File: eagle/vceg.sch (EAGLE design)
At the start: 58 parts, among them IC1 4052N, IC2 4001N, IC3 TL074P, IC4 CA3080E, Q1 2N3906INLINE, Q2 2N3906INLINE, U1 POWER

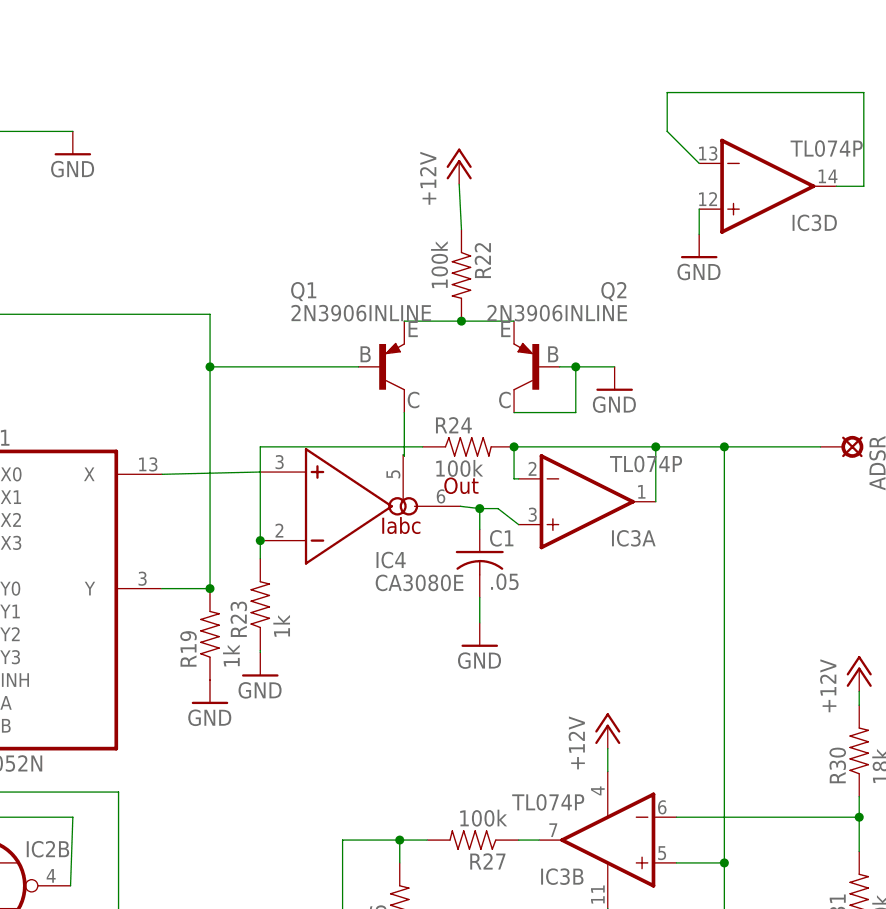
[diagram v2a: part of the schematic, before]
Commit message: ca3080 with power now
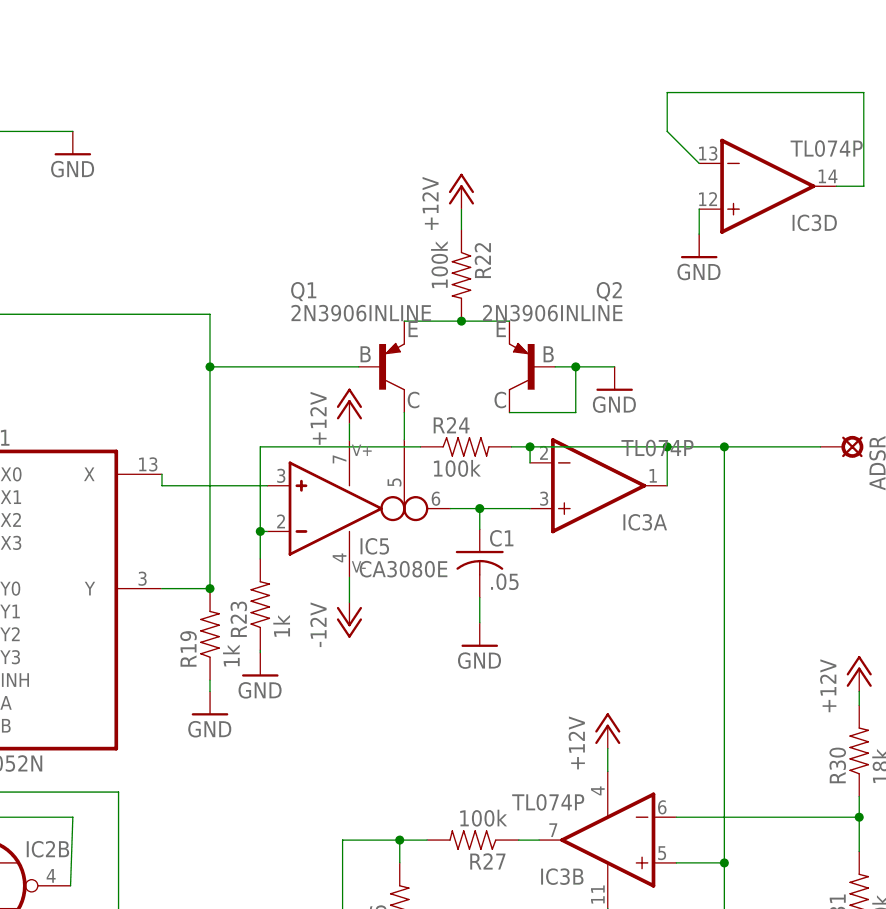
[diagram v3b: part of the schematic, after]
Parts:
- removed IC4: CA3080E, synthdiy:CA3080E
- added IC5: CA3080E, ota:CA3080E
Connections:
- removed net N$23: IC4.IABC, Q1.C
- new net N$41: IC1A.X, IC5G$1.IN_P
- net +12V: now also IC5G$2.V+
- net -12V: now also IC5G$2.V-
- net N$21: now also IC5G$1.I_BIAS, Q1.C; no longer IC1A.X, IC4.+IN
- net N$24: now also IC5G$1.IN_N; no longer IC4.-IN
- net N$28: now also IC5G$1.OUT; no longer IC4.OUT
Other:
- moved on the sheet: IC3A, Q2
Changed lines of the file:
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@@
 <part name="GND11" library="supply1" deviceset="GND" device=""/>
 <part name="R21" library="SparkFun-Resistors" deviceset="RESISTOR" device="PTH-1/4W" value="10k"/>
-<part name="IC4" library="synthdiy" deviceset="CA3080" device="E"/>
 <part name="Q1" library="bt_transistor" deviceset="2N3906" device="INLINE"/>
 <part name="Q2" library="bt_transistor" deviceset="2N3906" device="INLINE"/>
@@
 <part name="P+12" library="supply1" deviceset="+12V" device=""/>
 <part name="P-2" library="supply1" deviceset="-12V" device=""/>
+<part name="IC5" library="ota" deviceset="CA3080" device="E"/>
+<part name="P+13" library="supply1" deviceset="+12V" device=""/>
+<part name="P-3" library="supply1" deviceset="-12V" device=""/>
 </parts>
 <sheets>
@@
 <instance part="IC2" gate="C" x="67.818" y="-14.224"/>
 <instance part="IC2" gate="D" x="91.694" y="-22.352" rot="R180"/>
-<instance part="IC3" gate="A" x="133.35" y="55.372" rot="MR180"/>
+<instance part="IC3" gate="A" x="134.62" y="57.15" rot="MR180"/>
 <instance part="IC3" gate="B" x="135.636" y="17.78" rot="R180"/>
 <instance part="IC3" gate="C" x="135.636" y="-10.922" rot="R180"/>
@@
 <instance part="GND9" gate="1" x="48.26" y="27.94"/>
 <instance part="R19" gate="G$1" x="91.44" y="40.64" rot="R90"/>
-<instance part="GND10" gate="1" x="91.44" y="33.02"/>
+<instance part="GND10" gate="1" x="91.44" y="31.75"/>
 <instance part="GATE" gate="1" x="22.86" y="-8.636" rot="R90"/>
 <instance part="R20" gate="G$1" x="25.4" y="-16.51" rot="R90"/>
 <instance part="GND11" gate="1" x="25.4" y="-27.178"/>
 <instance part="R21" gate="G$1" x="37.592" y="12.7" rot="R180"/>
-<instance part="IC4" gate="G$1" x="107.188" y="54.864" rot="MR180"/>
 <instance part="Q1" gate="G$1" x="110.49" y="70.358"/>
-<instance part="Q2" gate="G$1" x="127.762" y="70.358" rot="MR0"/>
+<instance part="Q2" gate="G$1" x="127.254" y="70.358" rot="MR0"/>
 <instance part="R22" gate="G$1" x="119.38" y="80.518" rot="R270"/>
-<instance part="P+8" gate="1" x="119.126" y="93.218"/>
+<instance part="P+8" gate="1" x="119.38" y="90.424"/>
 <instance part="R23" gate="G$1" x="97.028" y="43.942" rot="R90"/>
 <instance part="GND12" gate="1" x="97.028" y="36.068"/>
-<instance part="R24" gate="G$1" x="120.142" y="61.468"/>
+<instance part="R24" gate="G$1" x="119.888" y="61.468"/>
 <instance part="C1" gate="G$1" x="121.412" y="49.784"/>
 <instance part="GND13" gate="1" x="121.412" y="39.37"/>
@@
 <instance part="P+12" gate="1" x="135.636" y="30.48"/>
 <instance part="P-2" gate="1" x="135.636" y="5.842"/>
+<instance part="IC5" gate="G$1" x="105.41" y="54.61"/>
+<instance part="IC5" gate="G$2" x="106.934" y="54.61"/>
+<instance part="P+13" gate="1" x="106.934" y="66.548"/>
+<instance part="P-3" gate="1" x="106.934" y="41.656"/>
 </instances>
 <busses>
@@
 <pinref part="R19" gate="G$1" pin="1"/>
 <pinref part="GND10" gate="1" pin="GND"/>
+<wire x1="91.44" y1="34.29" x2="91.44" y2="35.56" width="0.1524" layer="91"/>
 </segment>
 <segment>
@@
 <segment>
 <pinref part="Q2" gate="G$1" pin="C"/>
-<wire x1="125.222" y1="65.278" x2="132.08" y2="65.278" width="0.1524" layer="91"/>
+<wire x1="124.714" y1="65.278" x2="132.08" y2="65.278" width="0.1524" layer="91"/>
 <wire x1="132.08" y1="65.278" x2="132.08" y2="70.358" width="0.1524" layer="91"/>
-<wire x1="132.08" y1="70.358" x2="130.302" y2="70.358" width="0.1524" layer="91"/>
+<wire x1="132.08" y1="70.358" x2="129.794" y2="70.358" width="0.1524" layer="91"/>
 <pinref part="Q2" gate="G$1" pin="B"/>
 <pinref part="GND14" gate="1" pin="GND"/>
@@
 <pinref part="P+8" gate="1" pin="+12V"/>
 <pinref part="R22" gate="G$1" pin="1"/>
-<wire x1="119.126" y1="90.678" x2="119.38" y2="85.598" width="0.1524" layer="91"/>
+<wire x1="119.38" y1="87.884" x2="119.38" y2="85.598" width="0.1524" layer="91"/>
 </segment>
 <segment>
@@
 <wire x1="135.636" y1="27.94" x2="135.636" y2="25.4" width="0.1524" layer="91"/>
 </segment>
+<segment>
+<pinref part="IC5" gate="G$2" pin="V+"/>
+<pinref part="P+13" gate="1" pin="+12V"/>
+<wire x1="106.934" y1="64.008" x2="106.934" y2="62.23" width="0.1524" layer="91"/>
+</segment>
 </net>
 <net name="-12V" class="0">
@@
 <pinref part="P-2" gate="1" pin="-12V"/>
 <wire x1="135.636" y1="8.382" x2="135.636" y2="10.16" width="0.1524" layer="91"/>
+</segment>
+<segment>
+<pinref part="IC5" gate="G$2" pin="V-"/>
+<pinref part="P-3" gate="1" pin="-12V"/>
+<wire x1="106.934" y1="44.196" x2="106.934" y2="46.99" width="0.1524" layer="91"/>
 </segment>
 </net>
@@
 </segment>
 </net>
-<net name="N$21" class="0">
-<segment>
-<pinref part="IC1" gate="A" pin="X"/>
-<wire x1="86.106" y1="58.42" x2="97.028" y2="58.674" width="0.1524" layer="91"/>
-<pinref part="IC4" gate="G$1" pin="+IN"/>
-</segment>
-</net>
 <net name="N$22" class="0">
 <segment>
-<wire x1="125.222" y1="75.438" x2="119.38" y2="75.438" width="0.1524" layer="91"/>
+<wire x1="124.714" y1="75.438" x2="119.38" y2="75.438" width="0.1524" layer="91"/>
 <pinref part="R22" gate="G$1" pin="2"/>
 <wire x1="119.38" y1="75.438" x2="113.03" y2="75.438" width="0.1524" layer="91"/>
@@
 </segment>
 </net>
-<net name="N$23" class="0">
-<segment>
-<pinref part="Q1" gate="G$1" pin="C"/>
-<wire x1="113.03" y1="65.278" x2="113.03" y2="60.452" width="0.1524" layer="91"/>
-<wire x1="113.03" y1="60.452" x2="112.903" y2="60.579" width="0.1524" layer="91"/>
-<pinref part="IC4" gate="G$1" pin="IABC"/>
-</segment>
-</net>
 <net name="N$24" class="0">
 <segment>
-<pinref part="IC4" gate="G$1" pin="-IN"/>
 <pinref part="R23" gate="G$1" pin="2"/>
-<wire x1="97.028" y1="49.022" x2="97.028" y2="51.054" width="0.1524" layer="91"/>
 <pinref part="R24" gate="G$1" pin="1"/>
-<wire x1="115.062" y1="61.468" x2="97.028" y2="61.468" width="0.1524" layer="91"/>
-<wire x1="97.028" y1="61.468" x2="97.028" y2="51.054" width="0.1524" layer="91"/>
-<junction x="97.028" y="51.054"/>
+<wire x1="114.808" y1="61.468" x2="97.028" y2="61.468" width="0.1524" layer="91"/>
+<wire x1="97.028" y1="61.468" x2="97.028" y2="52.07" width="0.1524" layer="91"/>
+<pinref part="IC5" gate="G$1" pin="IN_N"/>
+<wire x1="97.028" y1="52.07" x2="97.028" y2="49.022" width="0.1524" layer="91"/>
+<wire x1="97.79" y1="52.07" x2="97.028" y2="52.07" width="0.1524" layer="91"/>
+<junction x="97.028" y="52.07"/>
 </segment>
 </net>
@@
 <segment>
 <pinref part="R24" gate="G$1" pin="2"/>
-<pinref part="IC3" gate="A" pin="-IN"/>
-<wire x1="125.222" y1="61.468" x2="125.222" y2="57.912" width="0.1524" layer="91"/>
-<wire x1="125.222" y1="57.912" x2="125.73" y2="57.912" width="0.1524" layer="91"/>
 <pinref part="IC3" gate="A" pin="OUT"/>
-<wire x1="140.97" y1="55.372" x2="140.97" y2="61.468" width="0.1524" layer="91"/>
-<wire x1="140.97" y1="61.468" x2="125.222" y2="61.468" width="0.1524" layer="91"/>
-<junction x="125.222" y="61.468"/>
+<wire x1="142.24" y1="57.15" x2="142.24" y2="61.468" width="0.1524" layer="91"/>
+<wire x1="142.24" y1="61.468" x2="127" y2="61.468" width="0.1524" layer="91"/>
 <pinref part="ADSR" gate="1" pin="MP"/>
+<wire x1="127" y1="61.468" x2="124.968" y2="61.468" width="0.1524" layer="91"/>
 <wire x1="159.258" y1="61.468" x2="148.59" y2="61.468" width="0.1524" layer="91"/>
-<junction x="140.97" y="61.468"/>
+<junction x="142.24" y="61.468"/>
 <pinref part="IC3" gate="C" pin="-IN"/>
-<wire x1="148.59" y1="61.468" x2="140.97" y2="61.468" width="0.1524" layer="91"/>
+<wire x1="148.59" y1="61.468" x2="142.24" y2="61.468" width="0.1524" layer="91"/>
 <wire x1="143.256" y1="-8.382" x2="148.59" y2="-8.382" width="0.1524" layer="91"/>
 <wire x1="148.59" y1="-8.382" x2="148.59" y2="15.24" width="0.1524" layer="91"/>
@@
 <wire x1="143.256" y1="15.24" x2="148.59" y2="15.24" width="0.1524" layer="91"/>
 <junction x="148.59" y="15.24"/>
+<pinref part="IC3" gate="A" pin="-IN"/>
+<wire x1="127" y1="59.69" x2="127" y2="61.468" width="0.1524" layer="91"/>
+<junction x="127" y="61.468"/>
 </segment>
 </net>
@@
 <segment>
 <pinref part="IC3" gate="A" pin="+IN"/>
-<wire x1="119.253" y1="54.864" x2="121.412" y2="54.61" width="0.1524" layer="91"/>
-<wire x1="121.412" y1="54.61" x2="123.444" y2="54.61" width="0.1524" layer="91"/>
-<wire x1="123.444" y1="54.61" x2="125.73" y2="52.832" width="0.1524" layer="91"/>
+<wire x1="121.412" y1="54.61" x2="127" y2="54.61" width="0.1524" layer="91"/>
 <pinref part="C1" gate="G$1" pin="1"/>
 <wire x1="121.412" y1="52.324" x2="121.412" y2="54.61" width="0.1524" layer="91"/>
+<pinref part="IC5" gate="G$1" pin="OUT"/>
+<wire x1="118.11" y1="54.61" x2="121.412" y2="54.61" width="0.1524" layer="91"/>
 <junction x="121.412" y="54.61"/>
-<pinref part="IC4" gate="G$1" pin="OUT"/>
 </segment>
 </net>
@@
 </segment>
 </net>
+<net name="N$21" class="0">
+<segment>
+<pinref part="Q1" gate="G$1" pin="C"/>
+<pinref part="IC5" gate="G$1" pin="I_BIAS"/>
+<wire x1="113.03" y1="65.278" x2="113.03" y2="62.23" width="0.1524" layer="91"/>
+</segment>
+</net>
+<net name="N$41" class="0">
+<segment>
+<pinref part="IC5" gate="G$1" pin="IN_P"/>
+<pinref part="IC1" gate="A" pin="X"/>
+<wire x1="97.79" y1="57.15" x2="86.106" y2="57.15" width="0.1524" layer="91"/>
+<wire x1="86.106" y1="57.15" x2="86.106" y2="58.42" width="0.1524" layer="91"/>
+</segment>
+</net>

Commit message: decoupling caps
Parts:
- added C4, C5, C6, C7, C8, C9: .1, rcl:C-US025-024X044
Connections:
- net +12V: now also C4.1, C5.1, C6.1, C8.1, IC1P.VCC, IC2P.VDD
- net -12V: now also C7.2, C9.2
- net GND: now also C4.2, C5.2, C6.2, C7.1, C8.2, C9.1, IC1P.GND, IC1P.VEE, IC2P.VSS
- net N$25: now also C3.2; no longer LFO_SW_1.MP
- net N$32: now also LFO_SW_2.MP; no longer C3.1
- net N$35: now also C3.1, LFO_SW_1.MP; no longer C3.2, LFO_SW_2.MP
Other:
- moved on the sheet: ADSR, ATTACK, ATT_POT, C1, C2, C3, DECAY, DEC_POT, GATE, GATE_NORMAL, IC1, IC2A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

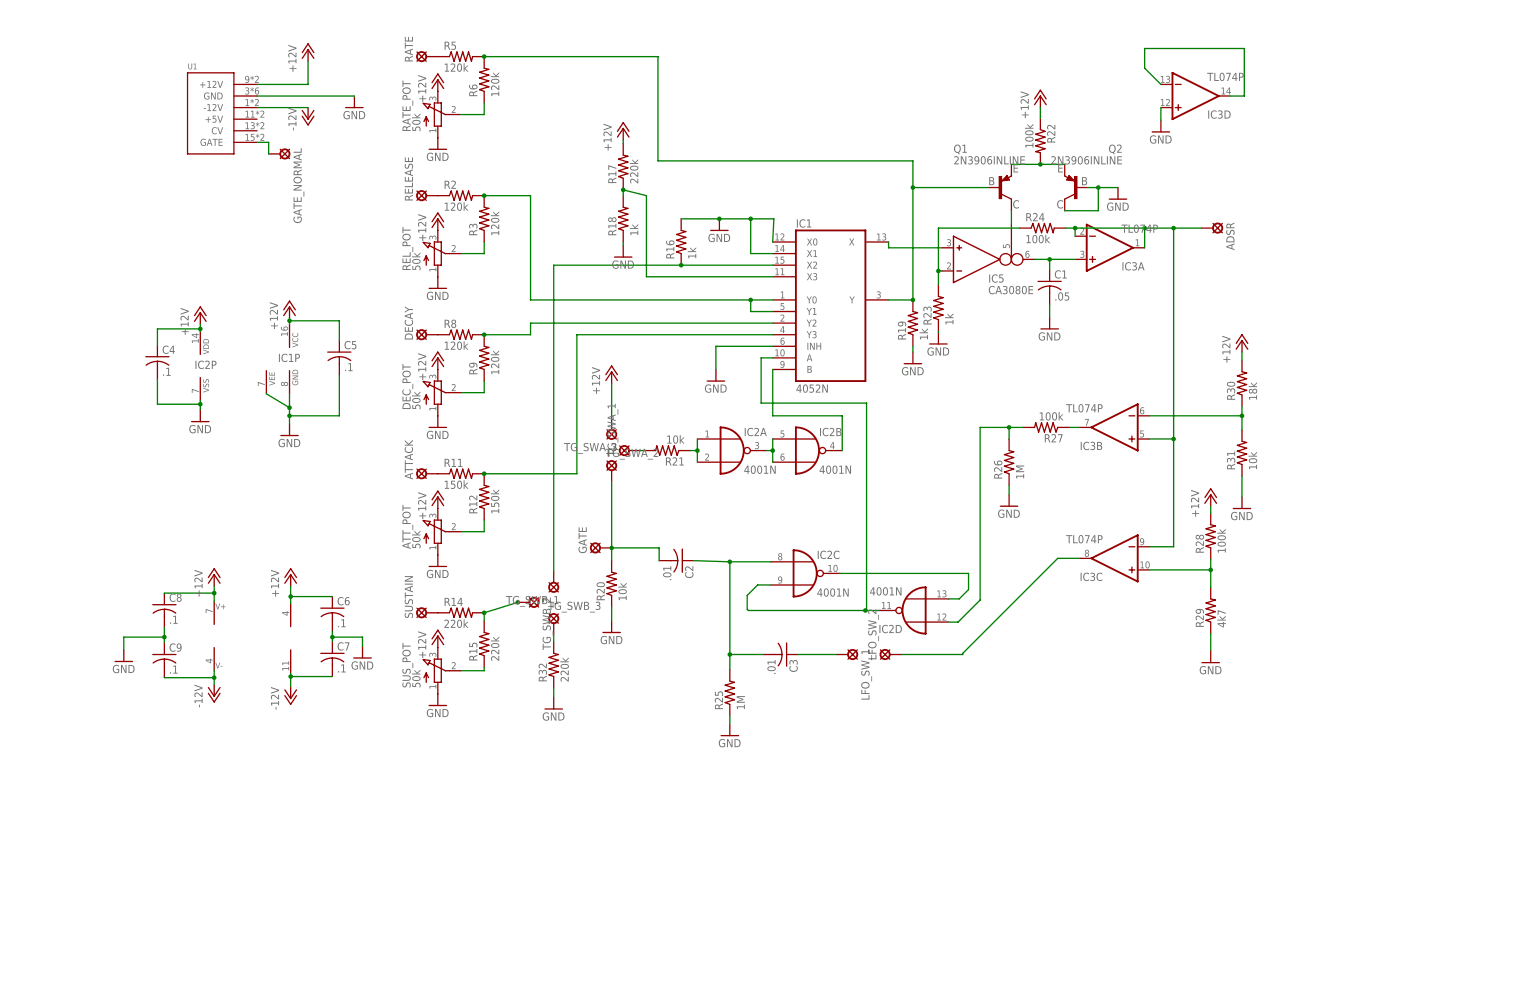
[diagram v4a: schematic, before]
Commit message: fixed schematic and board for 10k between 3906 and 3080
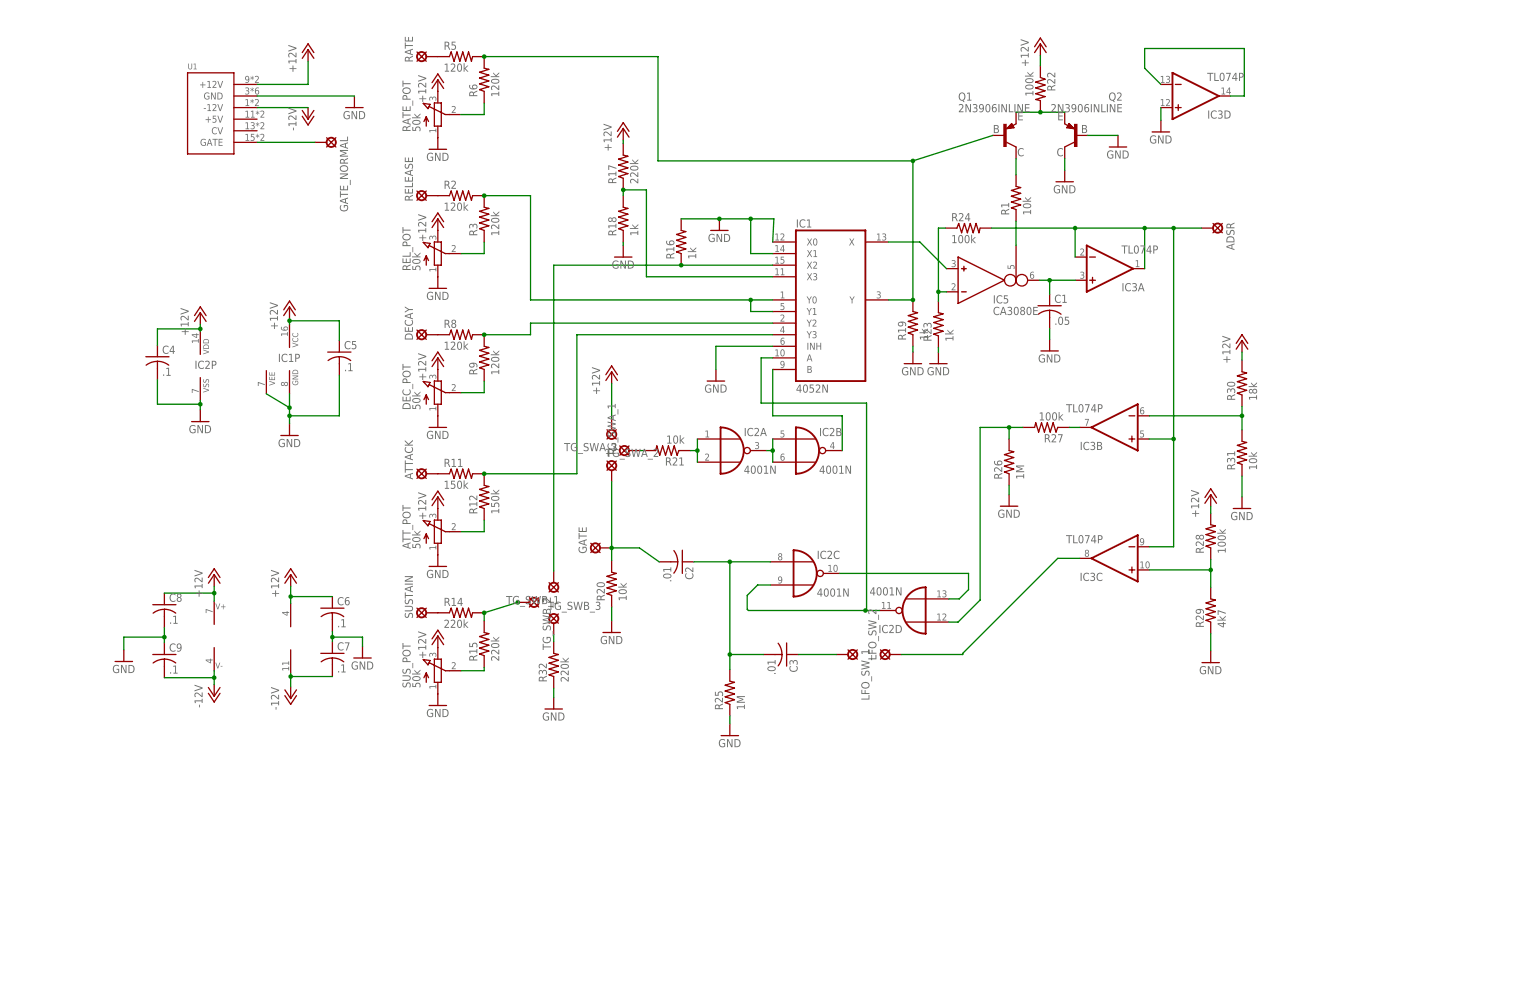
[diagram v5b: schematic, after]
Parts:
- added R1: 10k, SparkFun-Resistors:RESISTORPTH-1/4W
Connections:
- new net N$39: IC5G$1.I_BIAS, R1.1
- net N$21: now also R1.2; no longer IC5G$1.I_BIAS
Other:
- moved on the sheet: C1, GATE_NORMAL, IC3A, IC5, Q1, Q2, R22, R23, R24
